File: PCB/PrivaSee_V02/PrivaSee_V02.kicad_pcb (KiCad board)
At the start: 2 copper layers, 69.8 x 90 mm, 26 parts, among them J1 RFPC-SMA27-F, J2 Batt_Solder_Point, J3 Conn_02x06_Odd_Even, SW1 (Generic toggle state switch), U1 RC1602A, U2 LM358, U3 254, U4 DFR0568, U6 ESP32-C5-DevKitC-1

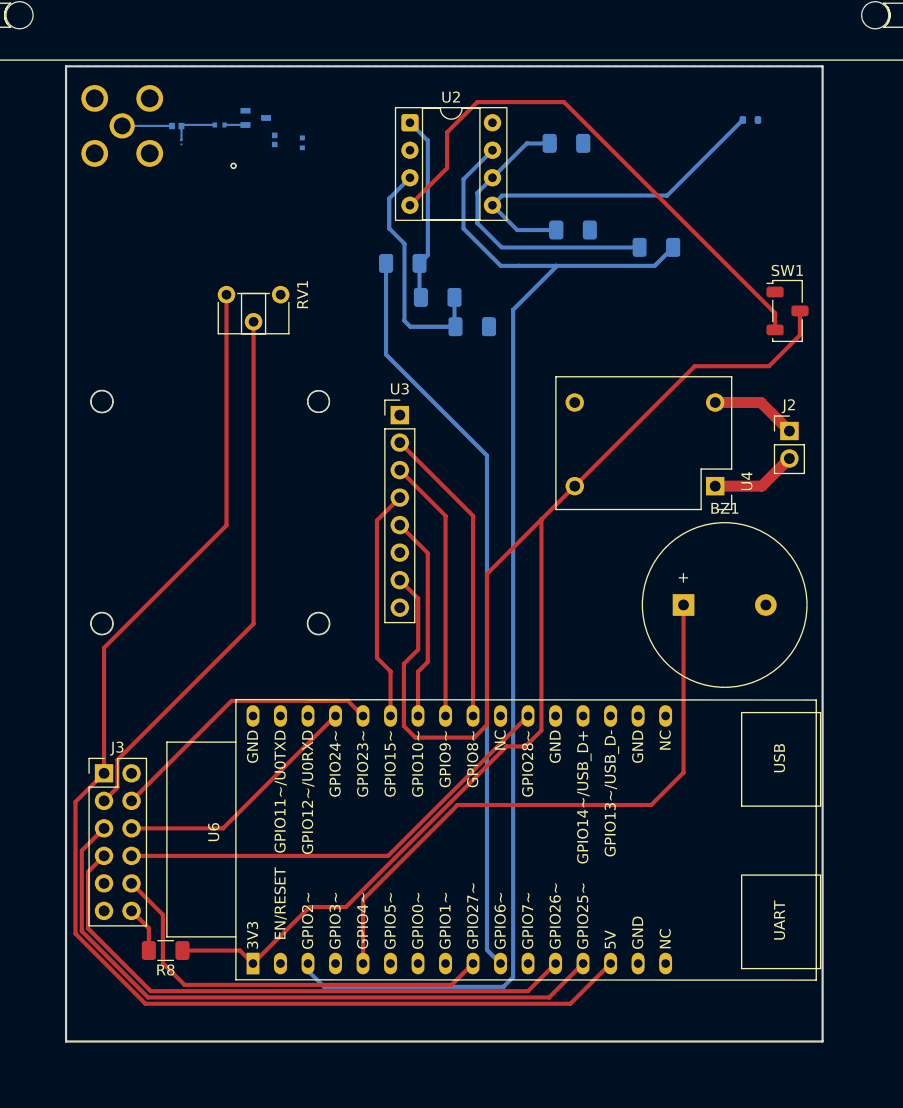
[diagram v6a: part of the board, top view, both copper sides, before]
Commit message: Trace Strip Implemented
Found a way to combine the RF taper tool + polygon shapes to make what I think is an appropriate taper.
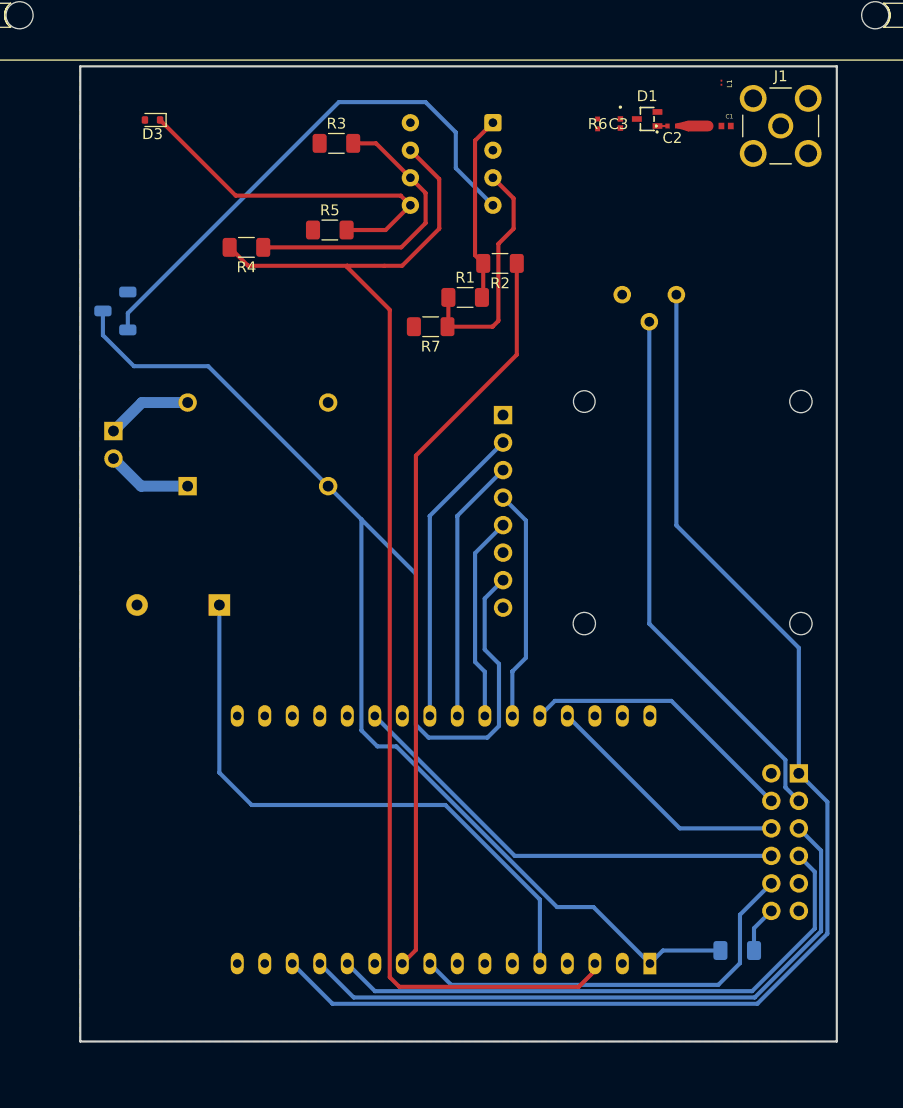
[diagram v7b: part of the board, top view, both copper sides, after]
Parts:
- BZ1, J2, J3, R8, RV1, SW1, U2, U3, U4, U6: moved to B.Cu
- C1, C2, C3, D1, D3, J1, L1, R1, R2, R3, R4, R5, R6, R7: moved to F.Cu
- moved J3 64.2 mm to (134.2, 86.9), turned to 180 degrees
- moved J2 62.4 mm to (70.9, 55.3), turned to 180 degrees
- moved SW1 62.1 mm to (71.1, 44.2), turned to 180 degrees
- moved J1 60.8 mm to (132.5, 27.1)
- moved D3 55.2 mm to (74.5, 26.5), turned to 180 degrees
- moved R8 52.8 mm to (128.5, 103.2), turned to 0 degrees
- moved C1 50.7 mm to (127.5, 27.1), turned to 0 degrees
- moved L1 50.2 mm to (127.0, 23.1), turned to -90 degrees
- moved U4 49.1 mm to (77.6, 61.2)
- moved BZ1 42.9 mm to (80.7, 71.3), turned to 180 degrees
- moved C2 41.8 mm to (122.5, 27.1), turned to 0 degrees
- moved R4 37.9 mm to (83.2, 38.3), turned to 180 degrees
- moved U6 36.6 mm to (120.4, 104.5)
- moved D1 36.1 mm to (120.2, 26.4), turned to 0 degrees
- moved C3 32.0 mm to (117.7, 26.9)
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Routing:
- net Net-(C1-Pad2): track 4.60 -> 0.01 mm
- net Net-(C1-Pad1): track 4.44 -> 1.80 mm
- net Net-(D1-A): track 1.94 -> 0.94 mm
- net (no net): vias 1 -> 0
- added copper zone on F.Cu, net GND
- removed copper zone on B.Cu, net GND

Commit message: flipped
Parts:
- BZ1, J2, J3, R8, RV1, SW1, U2, U3, U4, U6: moved to F.Cu
- C1, C2, C3, D1, D3, J1, L1, R1, R2, R3, R4, R5, R6, R7: moved to B.Cu
- moved J3 64.2 mm to (70.0, 86.9), turned to 0 degrees
- moved J2 62.4 mm to (133.3, 55.3), turned to 0 degrees
- moved SW1 62.1 mm to (133.1, 44.2), turned to 0 degrees
- moved J1 60.8 mm to (71.7, 27.1)
- moved D3 55.2 mm to (129.7, 26.5), turned to 0 degrees
- moved R8 52.8 mm to (75.7, 103.2), turned to 180 degrees
- moved C1 50.7 mm to (76.7, 27.1), turned to 180 degrees
- moved L1 49.9 mm to (77.2, 23.1)
- moved U4 49.1 mm to (126.6, 61.2)
- moved BZ1 42.9 mm to (123.5, 71.3), turned to 0 degrees
- moved C2 40.8 mm to (81.7, 27.1), turned to 180 degrees
- moved R4 37.9 mm to (121.0, 38.3), turned to 0 degrees
- moved U6 36.6 mm to (83.8, 104.5)
- moved D1 36.1 mm to (84.0, 26.4), turned to 180 degrees
- moved RV1 31.5 mm to (86.3, 42.7)
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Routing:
- added copper zone on B.Cu, net GND
- removed copper zone on F.Cu, net GND
